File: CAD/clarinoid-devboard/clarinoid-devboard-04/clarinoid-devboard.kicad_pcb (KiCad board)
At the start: 2 copper layers, 131.5 x 95 mm, 121 parts, among them IC1 PCA9554APW,118, IC2 Injoinic IP5306 battery charge, IC4 CY8CMBR3108-LQXIT, J1 AudioOut, J10 MIDI IN, J11 MIDI OUT, J12 SSD1306, J14 touch_conn_capsense, J2 XKB_U262-16XN-4BVC11 USB-C re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, J20 CapTouchSlider3, J3 microSD SOFNG TF-15x15, J4 header_spi, J5 header_i2c, J6 header_i2c1, J7 header_power tap, SW1 SW_Push, SW2 SW_Push, SW3 SW_Push, SW4 SW_Push, SW5 SW_Push, SW6 SW_Push, SW7 RotaryEncoder_Switch_ABC12, SW8 DIP_x4 blue dac enable, SW9 DIP_x4 red power source, U1 PCM5102A, U10 Pressure1_0x28_I2C0, U11 TLV75733PDBV, U12 ssd1306_graphic, U2 Micromod outline, U3 APCI0108-P001A Teensy_4.0_Mic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, U4 MPR121, 0x5A, U5 decor padarray, U7 TLV75533PDBV, U8 6N138, U9 WS2812

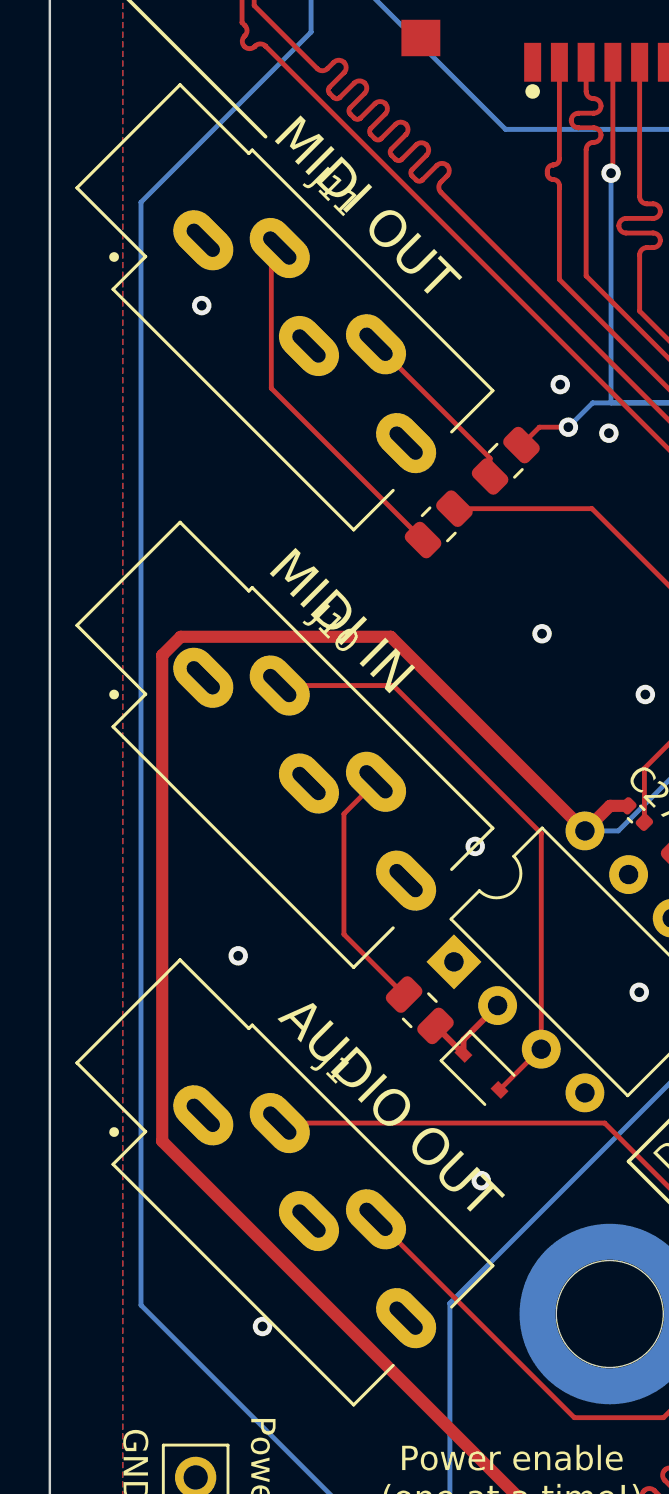
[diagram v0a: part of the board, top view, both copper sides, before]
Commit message: revision needed to production file: audio jack pin footprint was wrong orientation.
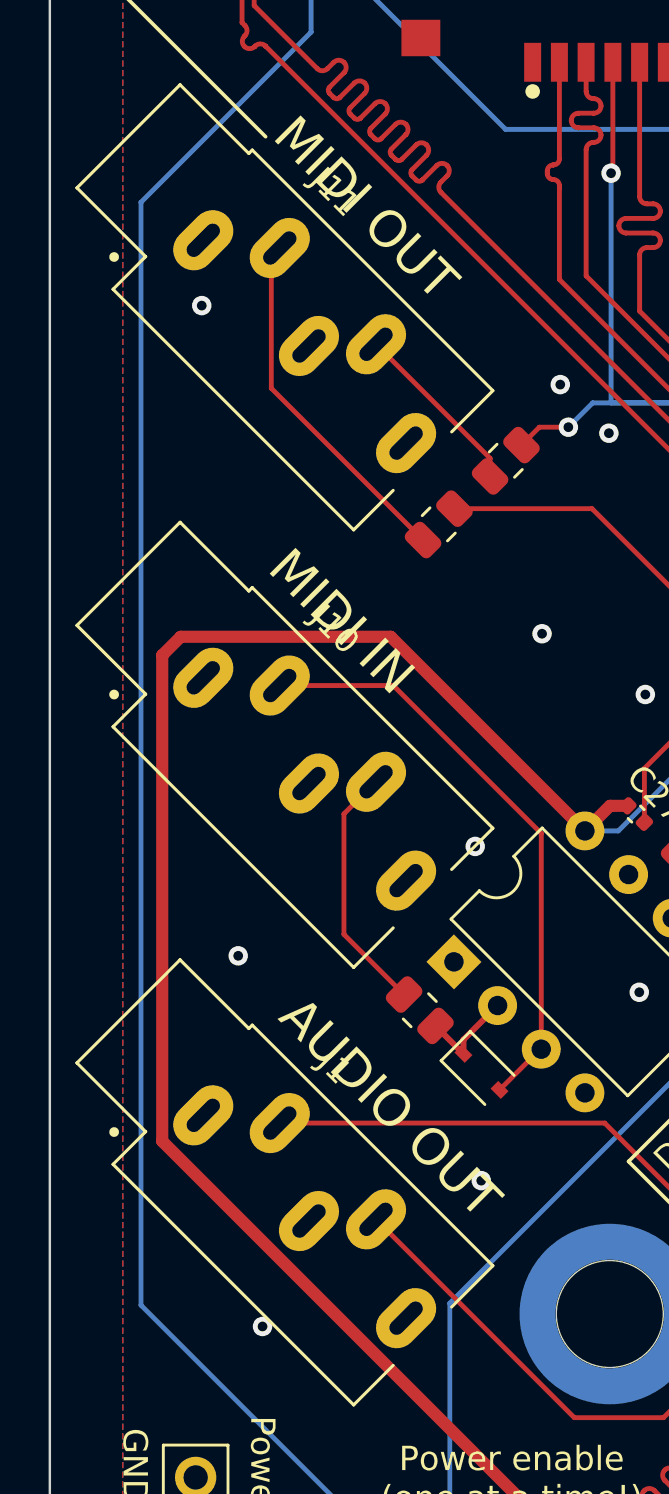
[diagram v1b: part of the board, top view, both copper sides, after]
